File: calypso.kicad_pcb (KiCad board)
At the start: 2 copper layers, 99.1 x 99.1 mm, 92 parts, among them IC1 RP2040_breakout, J1 Conn_02x05_Odd_Even, J10 AudioJack3, J11 AudioJack3, J13 Joy, J14 Video Out, J15 DB15_Female_HighDensity, J2 Conn_02x12_Odd_Even, J3 Mini-DIN-6, J4 Mini-DIN-6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

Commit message: Version 0.2
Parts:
- removed D8: BAT54S, Package_TO_SOT_SMD:SOT-23
- removed R23: 510, Resistor_SMD:R_1206_3216Metric_Pad1.30x1.75mm_HandSolder
- added SW2: SW_Push, Button_Switch_THT:SW_PUSH_6mm_H4.3mm, F.Cu at (115.9, 100.4)
- IC1: footprint rp2040:RP2040-Breakout -> rp2040:RP2040-Breakout_swd
- J1: value Conn_02x05_Odd_Even -> Conn_01x06; footprint Connector_PinHeader_2.54mm:PinHeader_2x05_P2.54mm_Vertical -> Connector_PinHeader_2.54mm:PinHeader_1x06_P2.54mm_Vertical
- J5: value Conn_01x03 -> Conn_01x05; footprint Connector_PinHeader_2.54mm:PinHeader_1x03_P2.54mm_Vertical -> Connector_PinHeader_2.54mm:PinHeader_1x05_P2.54mm_Vertical
- R4: value 10K -> 1K
- R45: value R -> 1K
- R6: value 10K -> 510
- moved D13 40.3 mm to (84.6, 85.4), turned to -90 degrees
- moved R45 31.2 mm to (89.9, 85.3), turned to -90 degrees
- moved J1 11.7 mm to (54.4, 54.6), turned to 90 degrees
- moved J5 2.69 mm to (80.0, 67.8)
- moved C3 0.80 mm to (107.7, 101.9)
- moved J2 0.80 mm to (122.2, 76.5)
- moved C2 0.73 mm to (107.9, 98.0)
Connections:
- IC1 pad 10: C10_M16 -> MIST_SS2
- IC1 pad 11: EXTA -> PS2_M_CLK
- IC1 pad 12: EXTB -> PS2_M_DAT
- IC1 pad 14: EXTC -> PS2_K_CLK
- IC1 pad 15: EXTD -> PS2_K_DAT
- IC1 pad 16: EXTE -> RP_AUX2
- IC1 pad 17: EXTF -> C10_R14
- IC1 pad 19: C10_F13 -> RP_AUX0
- IC1 pad 20: C10_F16 -> RP_AUX1
- IC1 pad 21: C10_F15 -> RP_GP16
- IC1 pad 27: RP_GP21 -> RP_AUX3
- IC1 pad 30: unconnected-(IC1-Pad30) -> RP_RESET
- IC1 pad 7: C10_R12 -> RP_GP5
- IC1 pad 9: C10_T15 -> MIST_CONF_DATA0
- J1 pad 1: RP_GP17 -> +3.3VP
- J1 pad 3: RP_GP18 -> RP_GP17
- J1 pad 4: +3.3VP -> RP_GP18
- J1 pad 5: RP_GP20 -> RP_GP19
- J1 pad 6: unconnected-(J1-Pad6) -> RP_GP20
- J13 pad 7: JOY_SELECT -> unconnected-(J13-Pad7)
- J2 pad 10: EXTD -> CYC_AUX2
- J2 pad 11: C10_P11 -> RP_AUX3
- J2 pad 12: EXTE -> C10_P14
- J2 pad 13: C10_R11 -> GND
- J2 pad 14: EXTF -> GND
- J2 pad 15: C10_T12 -> RP_GP0
- J2 pad 16: C10_T15 -> C10_J14
- J2 pad 17: C10_F13 -> RP_GP1
- J2 pad 18: C10_M16 -> C10_L2
- J2 pad 19: C10_F15 -> GND
- J2 pad 20: C10_F16 -> C10_F13
- J2 pad 21: +3.3VP -> RP_RESET
- J2 pad 22: +3.3VP -> C10_F16
- J2 pad 3: C10_R14 -> +3.3VP
- J2 pad 4: EXTA -> +3.3VP
- J2 pad 5: C10_P14 -> RP_AUX0
- J2 pad 6: EXTB -> C10_T12
- J2 pad 7: C10_J14 -> RP_AUX1
- J2 pad 8: EXTC -> C10_R11
- J2 pad 9: C10_L2 -> RP_AUX2
- J6 pad 2: C10_R12 -> RP_GP5
- R1 pad 1: C10_R12 -> RP_GP5
- R10 pad 1: EXTC -> PS2_K_CLK
- R11 pad 1: EXTD -> PS2_K_DAT
- R16 pad 2: C10_R11 -> C10_L16
- R17 pad 2: C10_R14 -> C10_J1
- R18 pad 2: C10_P14 -> C10_J2
- R19 pad 2: C10_J14 -> C10_P1
- R20 pad 2: C10_L2 -> C10_P2
- R8 pad 1: EXTA -> PS2_M_CLK
- R9 pad 1: EXTB -> PS2_M_DAT
- SW1 pad 4: IN_5V -> unconnected-(SW1-Pad4)
- SW1 pad 6: unconnected-(SW1-Pad6) -> IN_5V
- U2 pad 17: unconnected-(U2-Pad17) -> +3.3VP
- U3 pad 1.2: C10_R12 -> CYC_AUX2
- U3 pad 1.8: C10_T15 -> MIST_CONF_DATA0
- U3 pad 1.9: C10_M16 -> MIST_SS2
- U3 pad 6.2: C10_F15 -> RP_GP16
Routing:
- net C10_R12: track 159.4 -> 0.00 mm, vias 3 -> 0
- net RP_GP5: track 0.00 -> 111.2 mm, vias 0 -> 1
- net CYC_AUX2: track 0.00 -> 107.0 mm, vias 0 -> 2
- net RP_RESET: track 0.00 -> 96.6 mm, vias 0 -> 2
- net JOY_SELECT: track 88.5 -> 0.00 mm, vias 1 -> 0
- net C10_R14: track 115.7 -> 27.7 mm, vias 4 -> 1
- net C10_F15: track 72.4 -> 0.00 mm, vias 2 -> 0
- net C10_T15: track 71.3 -> 0.00 mm
- net RP_AUX3: track 0.00 -> 70.5 mm, vias 0 -> 2
- net C10_M16: track 67.2 -> 0.00 mm
- net EXTB: track 66.9 -> 0.00 mm, vias 2 -> 0
- net C10_P14: track 123.6 -> 64.9 mm, vias 2 -> 3
- net EXTA: track 57.3 -> 0.00 mm, vias 2 -> 0
- net EXTC: track 54.7 -> 0.00 mm, vias 3 -> 0
- net EXTD: track 52.7 -> 0.00 mm, vias 2 -> 0
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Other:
- board text added: "Calypso 0.2 overCLK & The RetroWiki FPGADev Team Aug 2024"
- board text added: "F13"
- board text added: "F16"
- board text added: "GP12"
- board text added: "GP14"
- board text added: "GP15"
- board text added: "GP21"
- board text added: "R12"
- board text added: "RST"
- board text added: "SRX"
- board text added: "STX"
- board text added: "SWD/UART"
- board text added: "SWDCLK"
- board text added: "SWDIO"
- board text added: "TCK"
- board text added: "TDI"
- board text added: "TDO"
- board text added: "TMS"
- board text removed: "CS1"
- board text removed: "CS2"
- board text removed: "Calypso 0.1 overCLK & The RetroWiki FPGADev Team Jun 2024"
- board text removed: "G10"
- board text removed: "G11"
- board text removed: "G13"
- board text removed: "G14"
- board text removed: "G8"
- board text removed: "G9"
- board text removed: "MISO"
- board text removed: "MOSI"
- board text removed: "P11"
- board text removed: "R14"
- board text removed: "RP SERIAL"
- board text removed: "SCLK"

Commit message: Corrected I2S capacitor values
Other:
- board text added: "Calypso 0.3-pre overCLK & The RetroWiki FPGADev Team Sep 2024"
- board text removed: "Calypso 0.2 overCLK & The RetroWiki FPGADev Team Aug 2024"
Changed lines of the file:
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@@
   (gr_line (start 84.836 60.706) (end 84.836 57.658) (layer "F.SilkS") (width 0.12))
   (gr_rect (start 25.4 20.32) (end 124.46 119.38) (layer "Edge.Cuts") (width 0.05) (fill none))
-  (gr_text "Calypso 0.2\noverCLK & The RetroWiki FPGADev Team\nAug 2024" (at 109.728 24.384) (layer "B.SilkS")
+  (gr_text "Calypso 0.3-pre\noverCLK & The RetroWiki FPGADev Team\nSep 2024" (at 109.728 24.384) (layer "B.SilkS")
     (effects (font (size 1 1) (thickness 0.15)) (justify left mirror))
   )

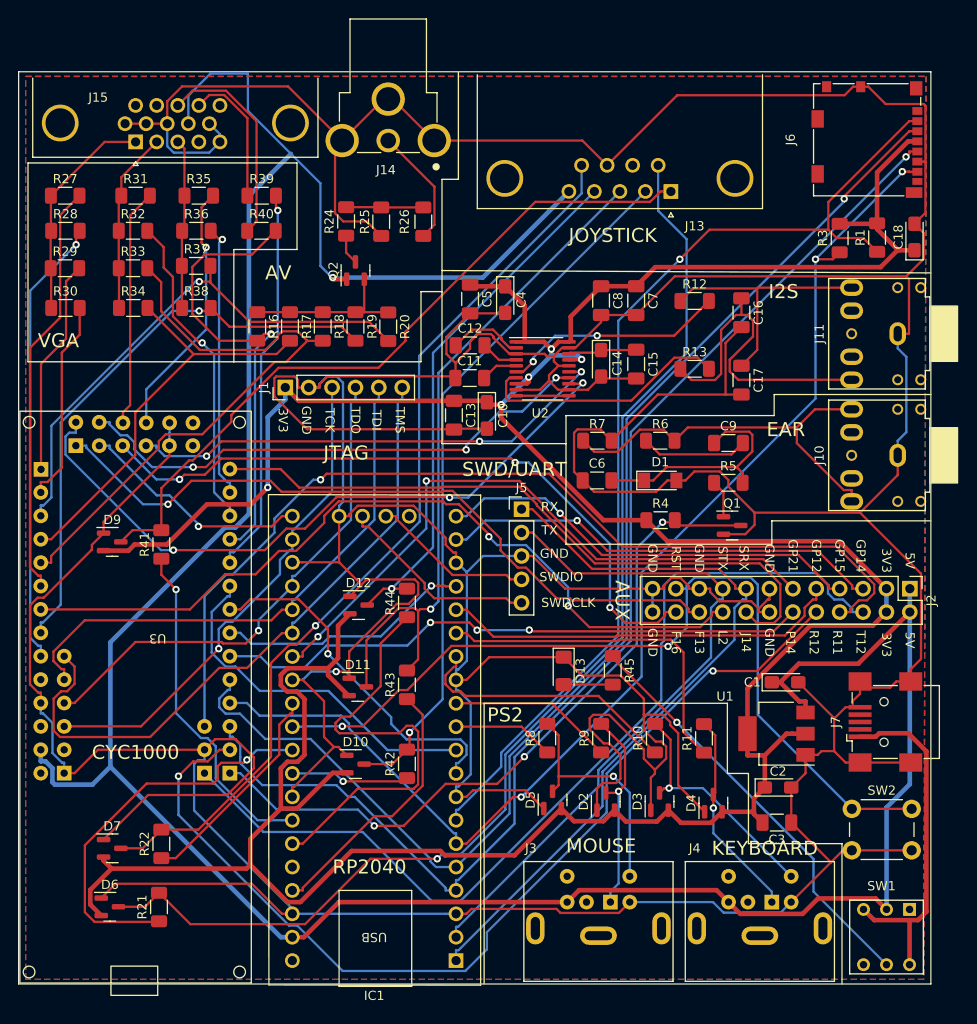
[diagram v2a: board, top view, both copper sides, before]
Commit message: Fix Q2 pinout & layout
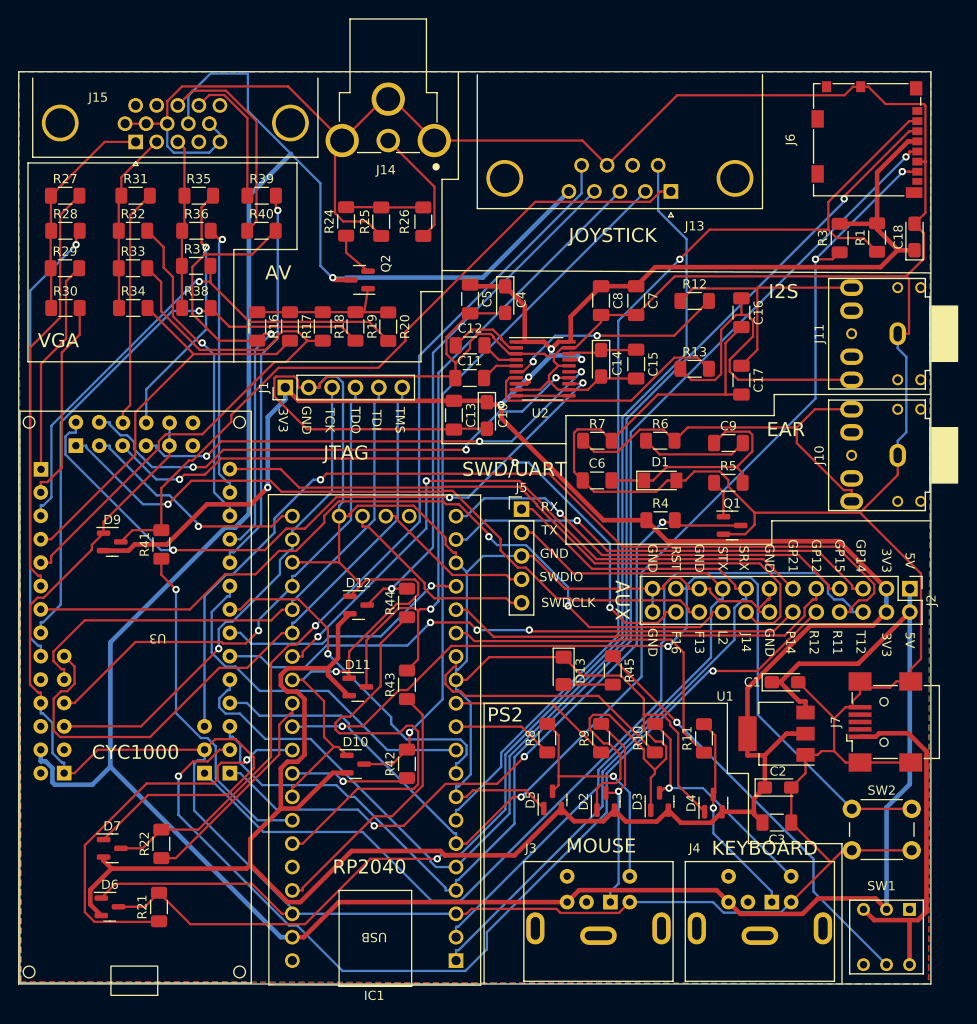
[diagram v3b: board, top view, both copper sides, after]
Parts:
- C16, C17: value 2.2uF -> 2.2nF
- Q2: value BC547 -> BC846
- moved Q2 1.10 mm to (62.4, 42.9), turned to 180 degrees
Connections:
- net CYC_AUX2 renamed C10_R12
- net MIST_CONF_DATA0 renamed C10_T15
- net MIST_SS2 renamed C10_N16
- net RP_GP16 renamed C10_F15
- Q2 pad 1: +5V -> Net-(R16-Pad1)
- Q2 pad 2: Net-(Q2-Pad2) -> Net-(R24-Pad1)
- Q2 pad 3: Net-(Q2-Pad3) -> +5V
- R16 pad 1: Net-(Q2-Pad2) -> Net-(R16-Pad1)
- R17 pad 1: Net-(Q2-Pad2) -> Net-(R16-Pad1)
- R18 pad 1: Net-(Q2-Pad2) -> Net-(R16-Pad1)
- R19 pad 1: Net-(Q2-Pad2) -> Net-(R16-Pad1)
- R20 pad 1: Net-(Q2-Pad2) -> Net-(R16-Pad1)
- R24 pad 1: Net-(Q2-Pad3) -> Net-(R24-Pad1)
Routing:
- net Net-(Q2-Pad2): track 17.8 -> 0.00 mm
- net Net-(R16-Pad1): track 0.00 -> 16.8 mm
- net Net-(R24-Pad1): track 0.00 -> 4.95 mm
- net Net-(Q2-Pad3): track 3.27 -> 0.00 mm
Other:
- board text added: "Calypso 0.3 overCLK & The RetroWiki FPGADev Team Sep 2024"
- board text removed: "Calypso 0.3-pre overCLK & The RetroWiki FPGADev Team Sep 2024"
